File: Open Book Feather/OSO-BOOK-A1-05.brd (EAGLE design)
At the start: 77.5 x 112.3 mm, 127 parts, among them J1 SJ-43514-SMT, J2 10118193-0001LF, Q1 DMG341, Q2 IRLML0100, SW1 SPDT_SWITCH, U1 AP2112-3.3, U2 MCP73831T-2ACI/OT, U3 ATSAMD51J64-TQFP(10X10), U4 GD25Q16C (or GD25Q32C), U5 74AC165D, U6 GD25Q16C (or GD25Q32C), U7 MAX4468EKAT, X1 JSTPH, X2 2x5 0.05" SWD

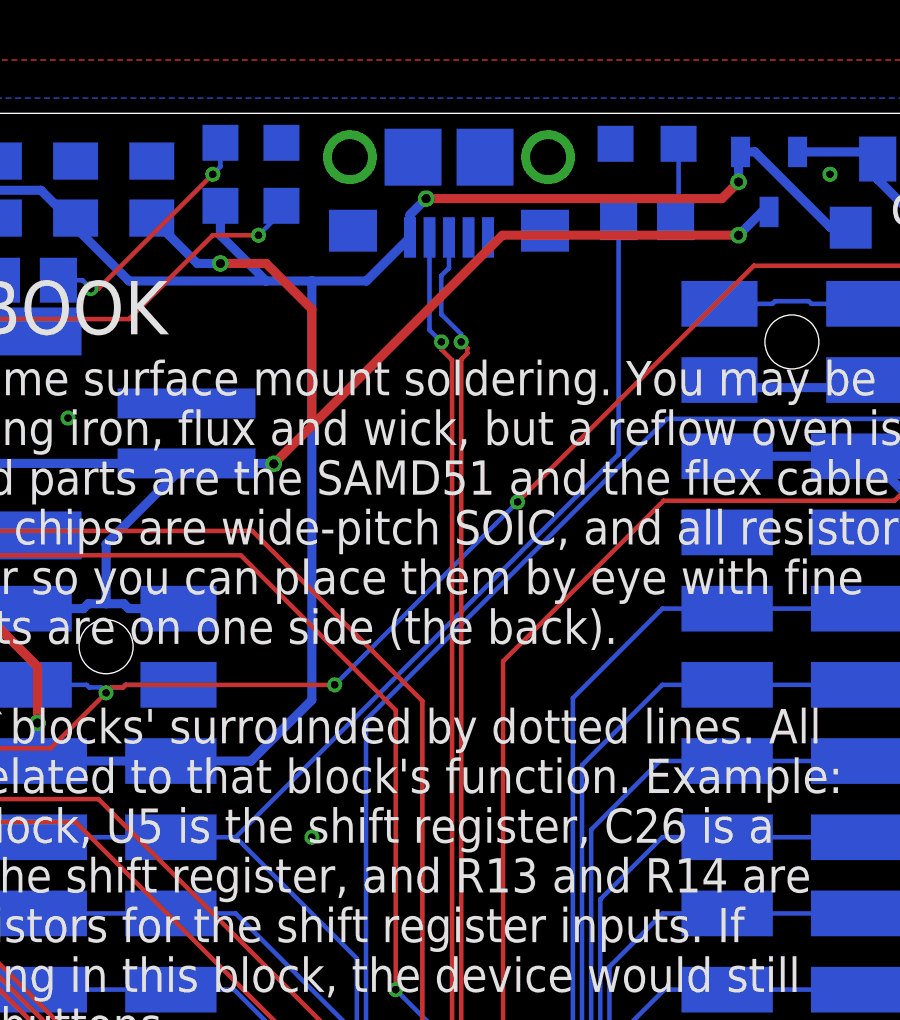
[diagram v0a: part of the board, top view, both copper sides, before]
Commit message: connect shield to ground via RC (reduce headphone noise?)
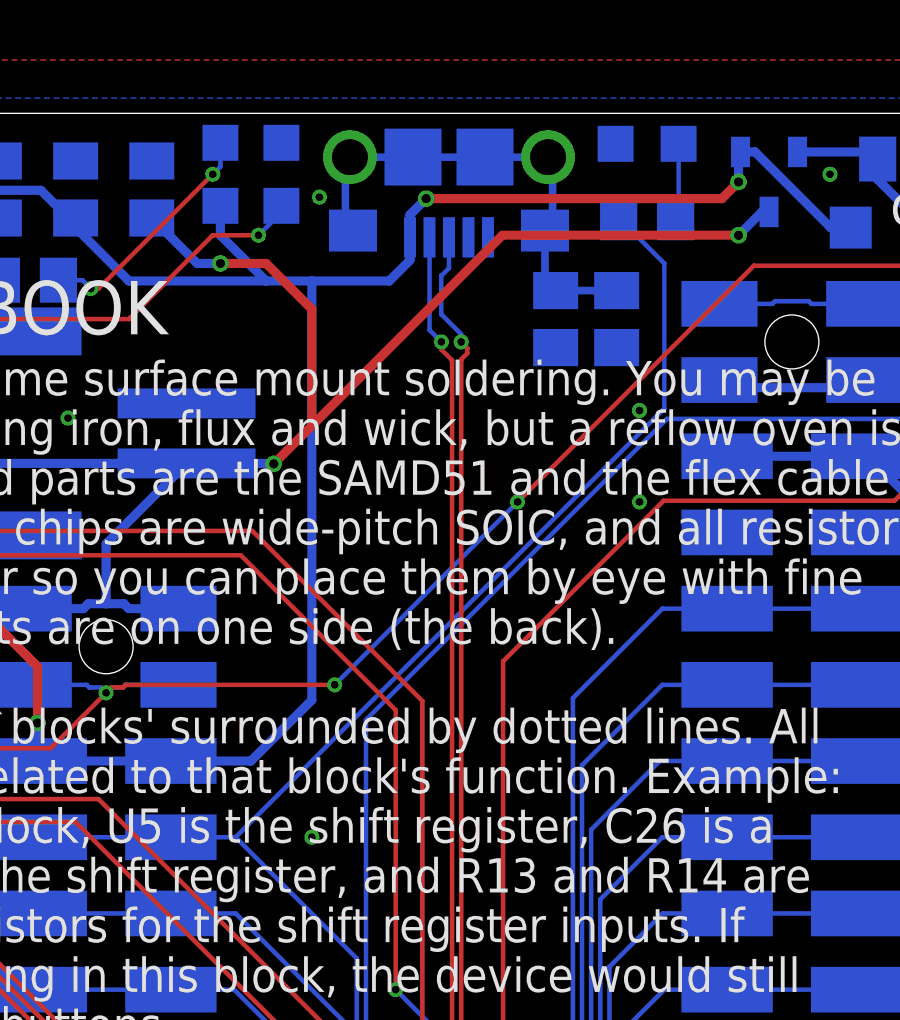
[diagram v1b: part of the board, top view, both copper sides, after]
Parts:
- added C29: 4.5nF, microbuilder:0805-NO
- added R27: 1M, microbuilder:0805-NO
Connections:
- new net SHIELD: C29.1, J2.S1, J2.S2, J2.S3, J2.S4, J2.S5, J2.S6, R27.1
- net GND: now also C29.2, R27.2; no longer J2.S1, J2.S2, J2.S3, J2.S4, J2.S5, J2.S6
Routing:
- net SHIELD: track 0.00 -> 16.0 mm
- net D13: track 74.1 -> 75.4 mm
- net GND: vias 50 -> 53
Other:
- board text added: "&"
- board text added: "BATTERY CHARGING"
- board text removed: "BATTERY AND CHARGING"
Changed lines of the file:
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@@
 <grid distance="0.01" unitdist="inch" unit="inch" style="lines" multiple="1" display="no" altdistance="0.001" altunitdist="inch" altunit="inch"/>
 <layers>
-<layer number="1" name="Top" color="4" fill="1" visible="yes" active="yes"/>
+<layer number="1" name="Top" color="4" fill="1" visible="no" active="yes"/>
 <layer number="2" name="Route2" color="1" fill="3" visible="no" active="no"/>
 <layer number="3" name="Route3" color="4" fill="3" visible="no" active="no"/>
@@
 <layer number="136" name="silktop" color="7" fill="1" visible="no" active="yes"/>
 <layer number="137" name="silkbottom" color="7" fill="1" visible="no" active="yes"/>
+<layer number="138" name="EEE" color="7" fill="1" visible="no" active="yes"/>
+<layer number="139" name="_tKeepout" color="7" fill="1" visible="no" active="yes"/>
+<layer number="140" name="mbKeepout" color="7" fill="1" visible="no" active="yes"/>
+<layer number="141" name="ASSEMBLY_TOP" color="7" fill="1" visible="no" active="yes"/>
+<layer number="142" name="mbRestrict" color="7" fill="1" visible="no" active="yes"/>
+<layer number="143" name="PLACE_BOUND_TOP" color="7" fill="1" visible="no" active="yes"/>
 <layer number="144" name="Drill_legend" color="7" fill="1" visible="no" active="yes"/>
 <layer number="145" name="DrillLegend_01-16" color="2" fill="9" visible="no" active="yes"/>
 <layer number="146" name="DrillLegend_01-20" color="7" fill="1" visible="no" active="yes"/>
+<layer number="147" name="PIN_NUMBER" color="7" fill="1" visible="no" active="yes"/>
+<layer number="149" name="DrillLegend_02-15" color="7" fill="1" visible="no" active="yes"/>
 <layer number="150" name="Notes" color="7" fill="1" visible="no" active="yes"/>
 <layer number="151" name="HeatSink" color="7" fill="1" visible="no" active="yes"/>
@@
 <layer number="166" name="AntennaArea" color="7" fill="1" visible="no" active="yes"/>
 <layer number="168" name="4mmHeightArea" color="7" fill="1" visible="no" active="yes"/>
+<layer number="191" name="mNets" color="7" fill="1" visible="no" active="yes"/>
+<layer number="192" name="mBusses" color="7" fill="1" visible="no" active="yes"/>
+<layer number="193" name="mPins" color="7" fill="1" visible="no" active="yes"/>
+<layer number="194" name="mSymbols" color="7" fill="1" visible="no" active="yes"/>
+<layer number="195" name="mNames" color="7" fill="1" visible="no" active="yes"/>
+<layer number="196" name="mValues" color="7" fill="1" visible="no" active="yes"/>
 <layer number="199" name="Contour" color="7" fill="1" visible="no" active="yes"/>
 <layer number="200" name="200bmp" color="1" fill="10" visible="no" active="no"/>
@@
 <wire x1="74.93" y1="0" x2="77.216" y2="2.286" width="0" layer="20" curve="90"/>
 <text x="76.708" y="107.061" size="1.27" layer="22" font="vector" ratio="18" rot="MR0" align="top-left">POWER SUPPLY</text>
-<text x="44.958" y="106.934" size="1.27" layer="22" font="vector" ratio="18" rot="MR0" align="top-left">BATTERY AND
+<text x="41.402" y="106.934" size="1.27" layer="22" font="vector" ratio="18" rot="MR0" align="top-left">BATTERY
 CHARGING</text>
 <text x="76.708" y="105.41" size="0.8128" layer="22" font="vector" rot="MR0" align="top-left">D1&amp;Q1 conspire to let
@@
 <wire x1="34.671" y1="108.585" x2="34.29" y2="108.966" width="0.1524" layer="22" style="shortdash"/>
 <wire x1="34.29" y1="108.966" x2="34.29" y2="112.141" width="0.1524" layer="22" style="shortdash"/>
+<text x="32.512" y="106.934" size="1.27" layer="22" font="vector" ratio="18" rot="MR0" align="top-left">&amp;</text>
 </plain>
 <attributes>
@@
 <attribute name="VALUE" x="66.0082" y="108.9142" size="0.4064" layer="28" ratio="10" rot="MR180"/>
 </element>
+<element name="C29" library="microbuilder" package="0805-NO" value="4.5nF" x="42.418" y="105.41" smashed="yes" rot="MR270">
+<attribute name="NAME" x="42.3926" y="103.505" size="0.508" layer="26" font="vector" ratio="18" rot="MR180" align="center"/>
+<attribute name="VALUE" x="43.18" y="103.378" size="0.4064" layer="28" ratio="10" rot="MR270"/>
+</element>
+<element name="R27" library="microbuilder" package="0805-NO" value="1M" x="44.45" y="105.41" smashed="yes" rot="MR270">
+<attribute name="NAME" x="44.3992" y="103.505" size="0.508" layer="26" font="vector" ratio="18" rot="MR180" align="center"/>
+<attribute name="VALUE" x="45.212" y="103.378" size="0.4064" layer="28" ratio="10" rot="MR270"/>
+</element>
 </elements>
 <signals>
@@
 <contactref element="U3" pad="47"/>
 <contactref element="U3" pad="54"/>
-<contactref element="J2" pad="S2"/>
-<contactref element="J2" pad="S5"/>
-<contactref element="J2" pad="S4"/>
-<contactref element="J2" pad="S3"/>
-<contactref element="J2" pad="S1"/>
-<contactref element="J2" pad="S6"/>
 <contactref element="U1" pad="2"/>
 <contactref element="C3" pad="2"/>
@@
 <contactref element="U6" pad="4"/>
 <contactref element="C28" pad="2"/>
-<contactref element="J2" pad="5"/>
 <contactref element="TP1" pad="P$1"/>
 <via x="24.892" y="10.16" extent="1-16" drill="0.254"/>
@@
 <contactref element="BTN_RESET" pad="P$1"/>
 <via x="17.018" y="7.366" extent="1-16" drill="0.254"/>
+<contactref element="R27" pad="2"/>
+<contactref element="C29" pad="2"/>
+<contactref element="J2" pad="5"/>
+<via x="45.212" y="102.362" extent="1-16" drill="0.254"/>
+<via x="45.212" y="99.314" extent="1-16" drill="0.254"/>
+<via x="34.544" y="109.474" extent="1-16" drill="0.254"/>
 </signal>
 <signal name="EINK_CS">
@@
 <wire x1="33.1564" y1="51.7824" x2="32.37863125" y2="51.7824" width="0.1524" layer="16"/>
 <wire x1="32.37863125" y1="51.7824" x2="30.607" y2="53.55403125" width="0.1524" layer="16"/>
-<wire x1="44.516" y1="100.904" x2="31.75" y2="88.138" width="0.1524" layer="16"/>
+<wire x1="46.04" y1="102.428" x2="31.75" y2="88.138" width="0.1524" layer="16"/>
 <wire x1="35.7886" y1="66.068375" x2="35.7886" y2="84.0994" width="0.1524" layer="16"/>
 <wire x1="31.75" y1="88.138" x2="29.591" y2="88.138" width="0.1524" layer="16"/>
@@
 <contactref element="MS1" pad="25'"/>
 <contactref element="MS1" pad="25"/>
-<wire x1="44.516" y1="108.7882" x2="44.516" y2="100.904" width="0.1524" layer="16"/>
+<wire x1="44.516" y1="108.7882" x2="46.04" y2="107.2642" width="0.1524" layer="16"/>
+<wire x1="46.04" y1="107.2642" x2="46.04" y2="102.428" width="0.1524" layer="16"/>
 </signal>
 <signal name="VBAT" class="1">
@@
 <contactref element="U2" pad="4"/>
 <contactref element="R2" pad="1"/>
-<wire x1="37.562" y1="108.1325" x2="36.1095" y2="106.68" width="0.3048" layer="16"/>
-<wire x1="36.1095" y1="106.68" x2="34.29" y2="106.68" width="0.3048" layer="16"/>
+<wire x1="37.562" y1="108.1325" x2="37.562" y2="107.3705" width="0.3048" layer="16"/>
+<wire x1="37.562" y1="107.3705" x2="36.8715" y2="106.68" width="0.3048" layer="16"/>
+<wire x1="36.8715" y1="106.68" x2="34.29" y2="106.68" width="0.3048" layer="16"/>
 <wire x1="34.29" y1="106.68" x2="32.766" y2="106.68" width="0.3048" layer="16"/>
 <wire x1="32.766" y1="106.68" x2="28.194" y2="106.68" width="0.3048" layer="16"/>
@@
 <wire x1="33.274" y1="108.966" x2="32.512" y2="108.204" width="0.1524" layer="16"/>
 </signal>
+<signal name="SHIELD" class="2">
+<contactref element="R27" pad="1"/>
+<contactref element="C29" pad="1"/>
+<contactref element="J2" pad="S6"/>
+<contactref element="J2" pad="S2"/>
+<contactref element="J2" pad="S3"/>
+<contactref element="J2" pad="S4"/>
+<contactref element="J2" pad="S5"/>
+<contactref element="J2" pad="S1"/>
+<wire x1="42.418" y1="106.36" x2="42.062" y2="106.716" width="0.254" layer="16"/>
+<wire x1="42.062" y1="106.716" x2="42.062" y2="108.3575" width="0.254" layer="16"/>
+<wire x1="42.164" y1="110.8075" x2="42.316" y2="110.6555" width="0.254" layer="16"/>
+<wire x1="42.062" y1="108.3575" x2="42.316" y2="108.6115" width="0.254" layer="16"/>
+<wire x1="42.316" y1="110.6555" x2="42.316" y2="108.6115" width="0.254" layer="16"/>
+<wire x1="42.164" y1="110.8075" x2="40.062" y2="110.8075" width="0.254" layer="16"/>
+<wire x1="40.062" y1="110.8075" x2="37.662" y2="110.8075" width="0.254" layer="16"/>
+<wire x1="37.662" y1="110.8075" x2="35.56" y2="110.8075" width="0.254" layer="16"/>
+<wire x1="35.56" y1="110.8075" x2="35.408" y2="110.6555" width="0.254" layer="16"/>
+<wire x1="35.408" y1="110.6555" x2="35.408" y2="108.6115" width="0.254" layer="16"/>
+<wire x1="35.408" y1="108.6115" x2="35.662" y2="108.3575" width="0.254" layer="16"/>
+<wire x1="44.45" y1="106.36" x2="42.418" y2="106.36" width="0.254" layer="16"/>
+</signal>
 </signals>

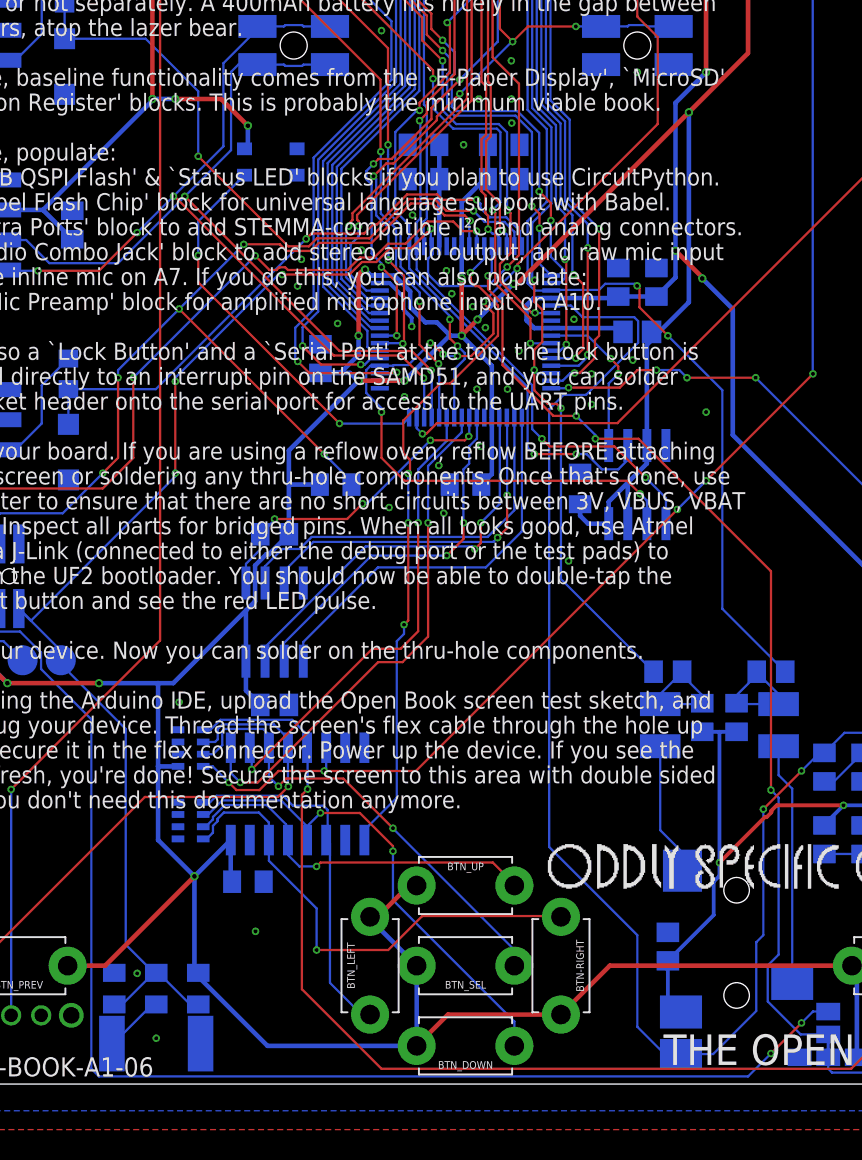
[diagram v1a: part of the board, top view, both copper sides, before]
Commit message: right angle neopixel near reset button
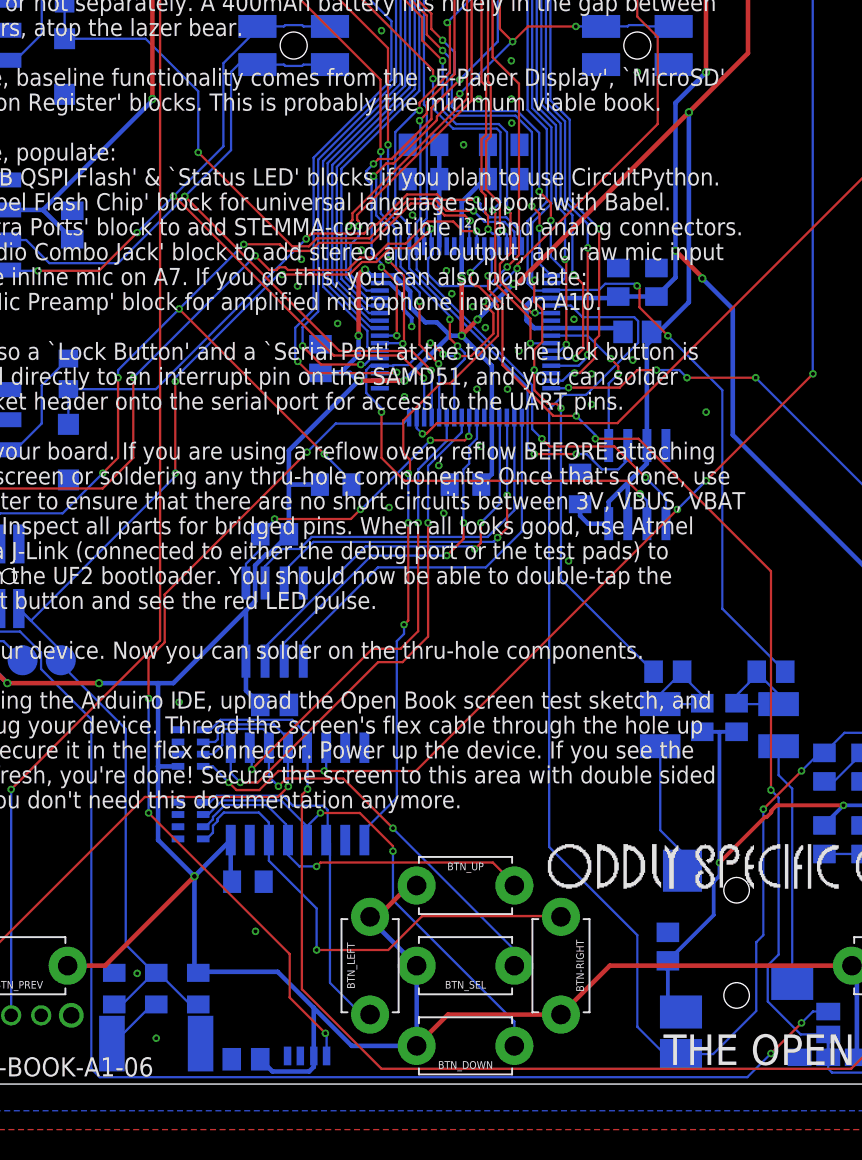
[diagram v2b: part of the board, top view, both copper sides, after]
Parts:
- removed STATUS: WS2812B3535, adafruit:LED3535
- added C36: 4.5nF, microbuilder:0805-NO
- added NEOPIX: WS2812B_4020, microbuilder:WS2812B_4020
- C29: value 4.5nF -> 1uF
- moved C29 105.3 mm to (24.3, 1.65), turned to 0 degrees
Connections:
- net +3V3: now also C29.1, NEOPIX.2; no longer STATUS.2
- net D8_NEOPIX: now also NEOPIX.1; no longer STATUS.1
- net GND: now also C36.2, NEOPIX.4; no longer STATUS.4
- net SHIELD: now also C36.1; no longer C29.1
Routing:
- net D8_NEOPIX: track 26.5 -> 57.2 mm, vias 2 -> 4
- net +3V3: track 513.9 -> 513.2 mm, vias 24 -> 22
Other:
- board text added: "NEOPIXEL=D8= PA15 (it's @ bottom by RESET."
- board text added: "R8 pulls !RESET high. Btn pulls it low; C13 & R9 help. Double tap for UF2 bootloader."
- board text removed: "NEOPIXEL=D8= PA15"
- board text removed: "R8 pulls !RESET high. Btn pulls it low. C13 is a filter cap. R9 discharges C13. Double tap for UF2 bootloader."
